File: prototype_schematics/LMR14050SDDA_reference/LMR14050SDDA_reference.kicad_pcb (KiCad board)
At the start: 2 copper layers, 11 parts, among them U1 LMR14050SDDA

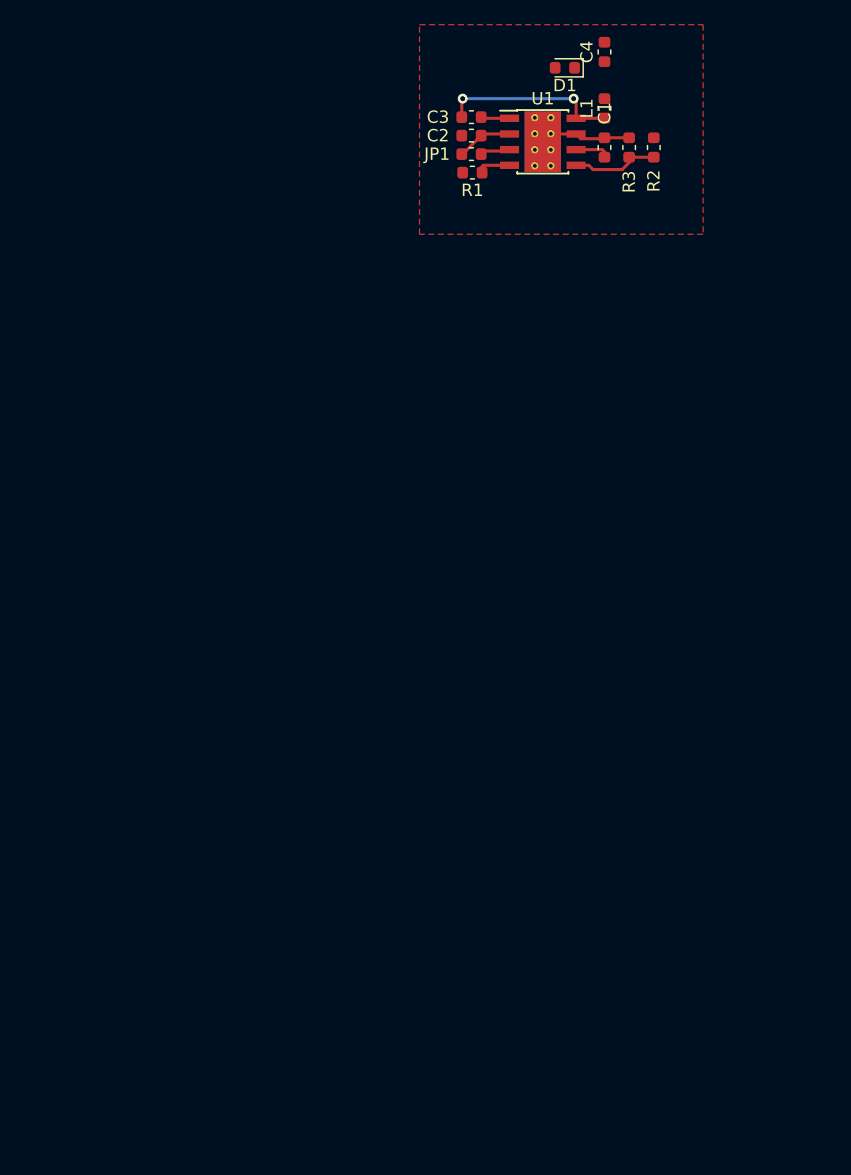
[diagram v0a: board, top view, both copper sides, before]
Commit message: WIP Add power distribution test board rev 1.
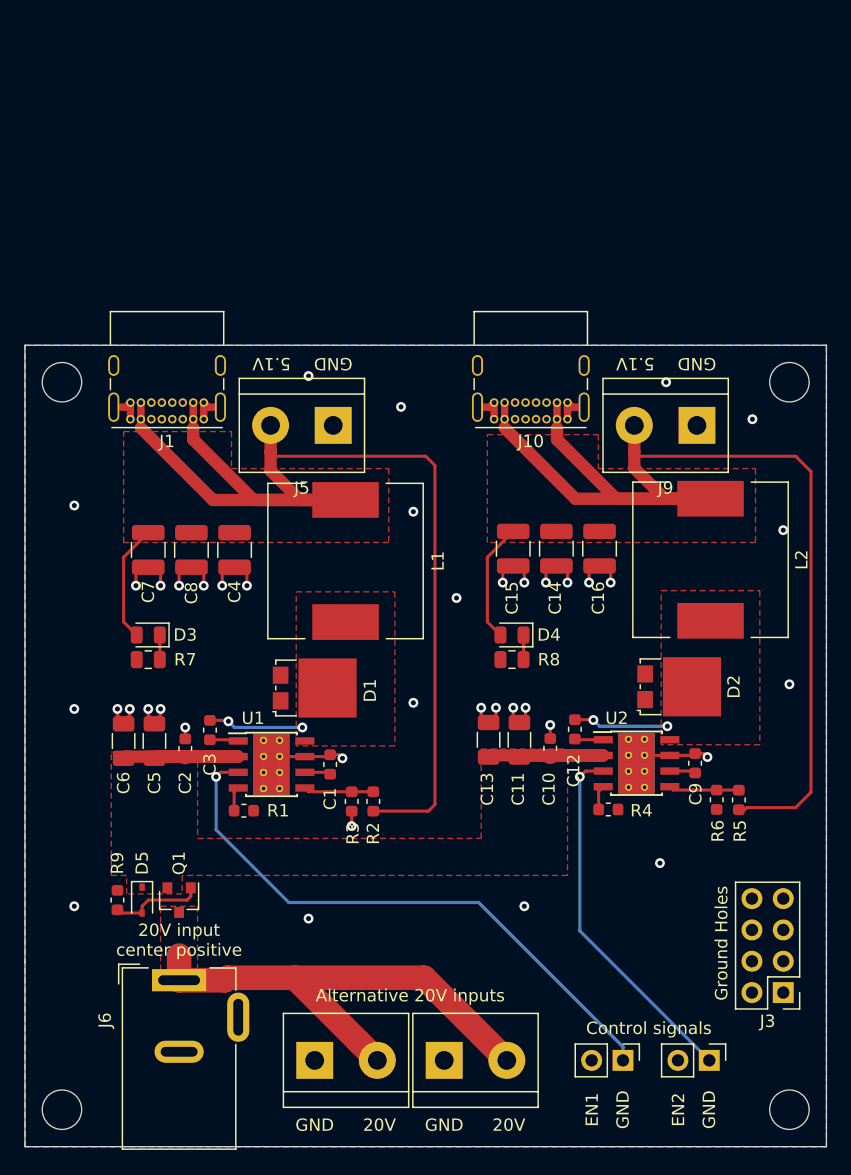
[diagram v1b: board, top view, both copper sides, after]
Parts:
- removed JP1: Jumper, Capacitor_SMD:C_0603_1608Metric
- added C10: 100n, Capacitor_SMD:C_0603_1608Metric, F.Cu at (137.6, 127.7)
- added C11: 4.7uF, Capacitor_SMD:C_1206_3216Metric, F.Cu at (135.1, 127.0)
- added C12: 100n, Capacitor_SMD:C_0603_1608Metric, F.Cu at (139.6, 126.2)
- added C13: 4.7uF, Capacitor_SMD:C_1206_3216Metric, F.Cu at (132.6, 127.0)
- added C14: 47uF, Capacitor_SMD:C_1210_3225Metric, F.Cu at (138.1, 111.5)
- added C15: 47uF, Capacitor_SMD:C_1210_3225Metric, F.Cu at (134.6, 111.5)
- added C16: 47uF, Capacitor_SMD:C_1210_3225Metric, F.Cu at (141.6, 111.5)
- added C5: 4.7uF, Capacitor_SMD:C_1206_3216Metric, F.Cu at (105.5, 127.1)
- added C6: 4.7uF, Capacitor_SMD:C_1206_3216Metric, F.Cu at (103.0, 127.1)
- added C7: 47uF, Capacitor_SMD:C_1210_3225Metric, F.Cu at (105.0, 111.6)
- added C8: 47uF, Capacitor_SMD:C_1210_3225Metric, F.Cu at (108.5, 111.6)
- added C9: 22nF, Capacitor_SMD:C_0603_1608Metric, F.Cu at (149.3, 128.9)
- added D2: D, Package_TO_SOT_SMD:TO-277A, F.Cu at (148.1, 122.7)
- added D3: LED, LED_SMD:LED_0805_2012Metric, F.Cu at (105.0, 118.5)
- added D4: LED, LED_SMD:LED_0805_2012Metric, F.Cu at (134.5, 118.5)
- added D5: 10V, Diode_SMD:D_SOD-323, F.Cu at (104.5, 140.0)
- added H1: MH, MountingHole:MountingHole_3.2mm_M3, F.Cu at (157.0, 98.0)
- added H2: MH, MountingHole:MountingHole_3.2mm_M3, F.Cu at (98.0, 157.0)
- added H3: MH, MountingHole:MountingHole_3.2mm_M3, F.Cu at (98.0, 98.0)
- added H4: MH, MountingHole:MountingHole_3.2mm_M3, F.Cu at (157.0, 157.0)
- added J1: USB_C_Receptacle_USB2.0, Connector_USB:USB_C_Receptacle_GCT_USB4085, F.Cu at (109.5, 101.0)
- added J10: USB_C_Receptacle_USB2.0, Connector_USB:USB_C_Receptacle_GCT_USB4085, F.Cu at (139.0, 101.0)
- added J2: Conn_EN, Connector_PinHeader_2.54mm:PinHeader_1x02_P2.54mm_Vertical, F.Cu at (143.5, 153.0)
- added J3: ground holes, Connector_PinHeader_2.54mm:PinHeader_2x04_P2.54mm_Vertical, F.Cu at (156.5, 147.5)
- added J4: V_in alt, TerminalBlock:TerminalBlock_bornier-2_P5.08mm, F.Cu at (129.0, 153.0)
- added J5: V_out alt, TerminalBlock:TerminalBlock_bornier-2_P5.08mm, F.Cu at (120.0, 101.5)
- added J6: DC_in, Connector_BarrelJack:BarrelJack_Wuerth_6941xx301002, F.Cu at (107.5, 146.5)
- added J7: Conn_EN, Connector_PinHeader_2.54mm:PinHeader_1x02_P2.54mm_Vertical, F.Cu at (150.5, 153.0)
- added J8: V_in alt, TerminalBlock:TerminalBlock_bornier-2_P5.08mm, F.Cu at (118.5, 153.0)
- added J9: V_out alt, TerminalBlock:TerminalBlock_bornier-2_P5.08mm, F.Cu at (149.5, 101.5)
- added L2: 8.2uH, Inductor_SMD:L_Wuerth_WE-PD-Typ-LS, F.Cu at (150.6, 112.4)
- added Q1: IRLML6344TRPBF, Package_TO_SOT_SMD:SOT-23, F.Cu at (107.5, 140.0)
- added R4: 84.5k, Resistor_SMD:R_0603_1608Metric, F.Cu at (142.3, 132.7)
- added R5: 100k, Resistor_SMD:R_0603_1608Metric, F.Cu at (152.9, 131.9)
- added R6: 17.8k, Resistor_SMD:R_0603_1608Metric, F.Cu at (151.1, 131.9)
- added R7: R, Resistor_SMD:R_0805_2012Metric, F.Cu at (105.0, 120.5)
- added R8: R, Resistor_SMD:R_0805_2012Metric, F.Cu at (134.5, 120.5)
- added R9: 100K, Resistor_SMD:R_0603_1608Metric, F.Cu at (102.5, 140.0)
- added U2: LMR14050SDDA, Package_SO:Texas_HSOP-8-1EP_3.9x4.9mm_P1.27mm_ThermalVias, F.Cu at (144.6, 128.9)
- C1: value TBD -> 22nF
- C3: value TDB -> 100n
- C4: value TDB -> 47uF; footprint Capacitor_SMD:C_0603_1608Metric -> Capacitor_SMD:C_1210_3225Metric
- D1: footprint Diode_SMD:D_0603_1608Metric -> Package_TO_SOT_SMD:TO-277A
- L1: value L -> 8.2uH; footprint Inductor_SMD:L_0603_1608Metric -> Inductor_SMD:L_Wuerth_WE-PD-Typ-LS
- R1: value TBD -> 84.5k
- R2: value R -> 100k
- R3: value R -> 17.8k
- moved R2 57.7 mm to (123.2, 132.0), turned to 90 degrees
- moved R3 57.6 mm to (121.5, 132.0), turned to 270 degrees
- moved U1 55.1 mm to (115.0, 129.0)
- moved R1 55.0 mm to (112.8, 132.8), turned to 0 degrees
- moved C2 54.9 mm to (108.0, 127.7), turned to 90 degrees
- moved C1 54.8 mm to (119.8, 129.0)
- moved D1 54.2 mm to (118.5, 122.8), turned to 90 degrees
- moved C3 54.0 mm to (110.0, 126.2), turned to 90 degrees
- moved C4 50.3 mm to (112.0, 111.6), turned to 270 degrees
- moved L1 42.3 mm to (121.0, 112.5)
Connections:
- net /V_FB renamed /V_FB1
- net /V_in renamed /V_in_protected
- net /V_out renamed /V_out1
- D1 pad 1: Net-(C3-Pad2) -> GND
- U1 pad 3: /enable_signal -> /en_signal1
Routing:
- net /V_out2: track 0.00 -> 106.4 mm
- net /V_out1: track 0.00 -> 105.3 mm
- net GND: track 7.45 -> 64.6 mm, vias 0 -> 40
- net /en_signal1: track 0.00 -> 47.6 mm, vias 0 -> 1
- net /V_in: track 0.00 -> 40.9 mm
- net /V_in_protected: track 4.55 -> 41.2 mm
- net /en_signal2: track 0.00 -> 29.4 mm, vias 0 -> 1
- net Net-(C12-Pad2): track 0.00 -> 7.72 mm, vias 0 -> 2
- net Net-(D5-Pad2): track 0.00 -> 7.64 mm
- net Net-(C3-Pad2): track 14.5 -> 7.74 mm
- net /V_FB2: track 0.00 -> 5.72 mm
- net /enable_signal: track 2.45 -> 0.00 mm
- net Net-(C12-Pad1): track 0.00 -> 2.32 mm
- net Net-(C9-Pad1): track 0.00 -> 2.11 mm
- net Net-(R4-Pad1): track 0.00 -> 2.00 mm
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- added copper zone on F.Cu, net /V_in
- added copper zone on F.Cu, net /V_in_protected
- added copper zone on F.Cu, net /V_out1
- added copper zone on F.Cu, net /V_out2
- added copper zone on B.Cu, net GND
- added copper zone on F.Cu, net Net-(C12-Pad2)
- added copper zone on F.Cu, net Net-(C3-Pad2)
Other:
- board outline added: 65 x 65 mm
- rule via_min_drill: 0.3 -> 0.2
- rule via_min_size: 0.4 -> 0.45
- board text added: "20V"
- board text added: "20V input center positive"
- board text added: "5.1V"
- board text added: "Alternative 20V inputs"
- board text added: "Control signals"
- board text added: "EN1"
- board text added: "EN2"
- board text added: "GND"
- board text added: "Ground Holes"
- board text added: "Special Computing Machine Power Distribution Test Board (rev. 1) Verneri Hirvonen (@asdvek) 2020"

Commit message: Final changes for ordering.
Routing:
- net Net-(C3-Pad2): track 7.74 -> 17.5 mm
- net GND: track 64.6 -> 73.6 mm, vias 40 -> 38
- net Net-(C12-Pad2): track 7.72 -> 15.6 mm
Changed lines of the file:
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@@
   (general
     (thickness 1.6)
-    (drawings 24)
-    (tracks 236)
+    (drawings 26)
+    (tracks 245)
     (zones 0)
     (modules 49)
@@
       (outputformat 1)
       (mirror false)
-      (drillshape 1)
+      (drillshape 0)
       (scaleselection 1)
-      (outputdirectory ""))
+      (outputdirectory "plots/"))
   )
   (net 0 "")
@@
     (tags resistor)
     (attr smd)
-    (fp_text reference R4 (at 2.6875 0.1) (layer F.SilkS)
+    (fp_text reference R4 (at -2.8125 0.1) (layer F.SilkS)
       (effects (font (size 1 1) (thickness 0.15)))
     )
@@
     (tags resistor)
     (attr smd)
-    (fp_text reference R1 (at 2.7875 0) (layer F.SilkS)
+    (fp_text reference R1 (at -2.75 0) (layer F.SilkS)
       (effects (font (size 1 1) (thickness 0.15)))
     )
@@
     )
   )
+  (gr_poly (pts (xy 146.4 133.8) (xy 144 133.8) (xy 144 131.6) (xy 146.4 131.6)) (layer F.Mask) (width 0.1))
+  (gr_poly (pts (xy 116.5 134) (xy 114.5 134) (xy 114.5 131.5) (xy 116.5 131.5)) (layer F.Mask) (width 0.1))
   (gr_poly (pts (xy 160 138) (xy 155.5 138) (xy 155.5 133.5) (xy 160 133.5)) (layer B.Mask) (width 0.1))
   (gr_poly (pts (xy 160 138) (xy 155.5 138) (xy 155.5 133.5) (xy 160 133.5)) (layer F.Mask) (width 0.1))
-  (gr_text "Special Computing Machine\nPower Distribution Test Board (rev. 1)\nVerneri Hirvonen (@asdvek) 2020" (at 153 105.5 90) (layer B.SilkS)
+  (gr_text "Special Computing Machine\nPower Distribution Test Board (rev. 1)\nVerneri Hirvonen (@asdvek) 2020" (at 99.6 152.4 270) (layer B.SilkS)
     (effects (font (size 1 1) (thickness 0.15)) (justify left mirror))
   )
@@
   (segment (start 147.3 128.265) (end 145.235 128.265) (width 0.25) (layer F.Cu) (net 1))
   (via (at 99 108) (size 0.8) (drill 0.4) (layers F.Cu B.Cu) (net 1))
-  (via (at 99 124.5) (size 0.8) (drill 0.4) (layers F.Cu B.Cu) (net 1))
-  (via (at 99 140.5) (size 0.8) (drill 0.4) (layers F.Cu B.Cu) (net 1))
   (via (at 118 141.5) (size 0.8) (drill 0.4) (layers F.Cu B.Cu) (net 1))
   (via (at 135.5 140.5) (size 0.8) (drill 0.4) (layers F.Cu B.Cu) (net 1))
@@
   (via (at 126.5 124) (size 0.8) (drill 0.4) (layers F.Cu B.Cu) (net 1))
   (via (at 126.5 108.5) (size 0.8) (drill 0.4) (layers F.Cu B.Cu) (net 1))
+  (segment (start 115 129) (end 115 131.5) (width 2) (layer F.Cu) (net 1))
+  (segment (start 115 131.5) (end 116.5 133) (width 2) (layer F.Cu) (net 1))
+  (segment (start 144.6 131.340002) (end 146 132.740002) (width 2) (layer F.Cu) (net 1))
+  (segment (start 144.6 128.9) (end 144.6 131.340002) (width 2) (layer F.Cu) (net 1))
   (segment (start 119.5975 129.635) (end 119.75 129.7875) (width 0.25) (layer F.Cu) (net 2))
   (segment (start 117.7 129.635) (end 119.5975 129.635) (width 0.25) (layer F.Cu) (net 2))
@@
   (segment (start 116.87999 146.29999) (end 127.37999 146.29999) (width 2) (layer F.Cu) (net 3))
   (segment (start 107.5 146.5) (end 107.5 144.5) (width 2) (layer F.Cu) (net 3))
-  (segment (start 137.81 128.265) (end 137.6 128.475) (width 1) (layer F.Cu) (net 35))
-  (segment (start 141.9 128.265) (end 137.81 128.265) (width 1) (layer F.Cu) (net 35))
-  (segment (start 135.235 128.265) (end 135.1 128.4) (width 1) (layer F.Cu) (net 35))
-  (segment (start 141.9 128.265) (end 135.235 128.265) (width 1) (layer F.Cu) (net 35))
-  (segment (start 132.735 128.265) (end 132.6 128.4) (width 1) (layer F.Cu) (net 35))
-  (segment (start 141.9 128.265) (end 132.735 128.265) (width 1) (layer F.Cu) (net 35))
   (via (at 117.5 126) (size 0.8) (drill 0.4) (layers F.Cu B.Cu) (net 4))
   (segment (start 117.5 126) (end 112 126) (width 0.25) (layer B.Cu) (net 4))
@@
   (segment (start 111.425 125.425) (end 111.5 125.5) (width 0.25) (layer F.Cu) (net 4))
   (segment (start 110 125.425) (end 111.425 125.425) (width 0.25) (layer F.Cu) (net 4))
+  (segment (start 119.54 122.8) (end 119.54 120.86) (width 1) (layer F.Cu) (net 4))
+  (segment (start 119.54 122.8) (end 119.54 120.06) (width 1) (layer F.Cu) (net 4))
+  (segment (start 121 117.45) (end 121 119.4) (width 1) (layer F.Cu) (net 4))
+  (segment (start 119.54 122.8) (end 119.54 125.94) (width 1) (layer F.Cu) (net 4))
   (segment (start 112.205 127) (end 112.3 127.095) (width 0.25) (layer F.Cu) (net 5))
   (segment (start 110 127) (end 112.205 127) (width 0.25) (layer F.Cu) (net 5))
@@
   (via (at 147.1 125.9) (size 0.8) (drill 0.4) (layers F.Cu B.Cu) (net 17))
   (segment (start 141.6 125.9) (end 147.1 125.9) (width 0.25) (layer B.Cu) (net 17))
+  (segment (start 149.1 122.7) (end 149.1 125.9) (width 1) (layer F.Cu) (net 17))
+  (segment (start 150.6 117.35) (end 150.6 119.2) (width 1) (layer F.Cu) (net 17))
+  (segment (start 149.1 122.7) (end 149.1 119.9) (width 1) (layer F.Cu) (net 17))
   (segment (start 139.6575 126.995) (end 139.6 126.9375) (width 0.25) (layer F.Cu) (net 18))
   (segment (start 141.9 126.995) (end 139.6575 126.995) (width 0.25) (layer F.Cu) (net 18))
@@
   (segment (start 105.9375 120.5) (end 105.9375 118.5) (width 0.25) (layer F.Cu) (net 33))
   (segment (start 135.4375 120.495) (end 135.4375 118.5) (width 0.25) (layer F.Cu) (net 34))
+  (segment (start 137.81 128.265) (end 137.6 128.475) (width 1) (layer F.Cu) (net 35))
+  (segment (start 141.9 128.265) (end 137.81 128.265) (width 1) (layer F.Cu) (net 35))
+  (segment (start 135.235 128.265) (end 135.1 128.4) (width 1) (layer F.Cu) (net 35))
+  (segment (start 141.9 128.265) (end 135.235 128.265) (width 1) (layer F.Cu) (net 35))
+  (segment (start 132.735 128.265) (end 132.6 128.4) (width 1) (layer F.Cu) (net 35))
+  (segment (start 141.9 128.265) (end 132.735 128.265) (width 1) (layer F.Cu) (net 35))
   (segment (start 108.135 128.365) (end 108 128.5) (width 1) (layer F.Cu) (net 35))
   (segment (start 112.3 128.365) (end 108.135 128.365) (width 1) (layer F.Cu) (net 35))

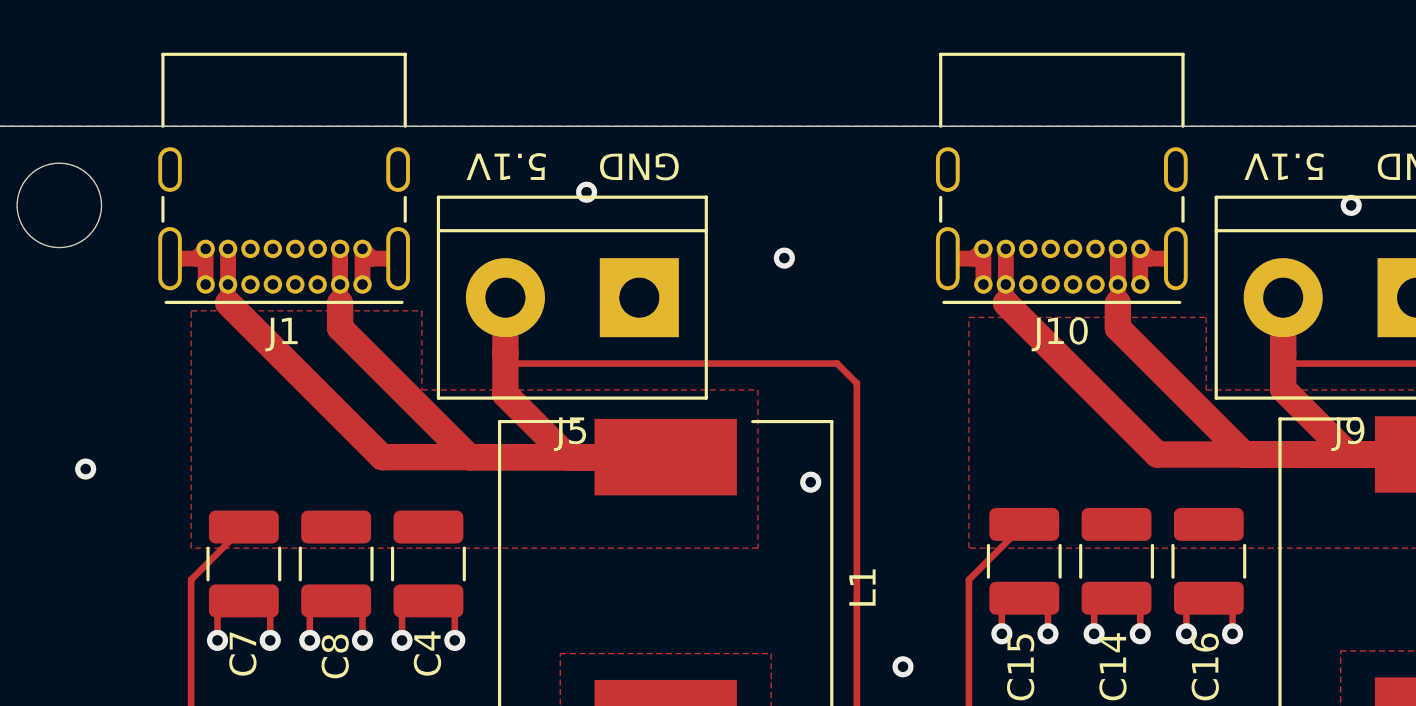
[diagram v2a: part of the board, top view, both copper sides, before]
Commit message: Change USB C receptacle to a component that's in stock.
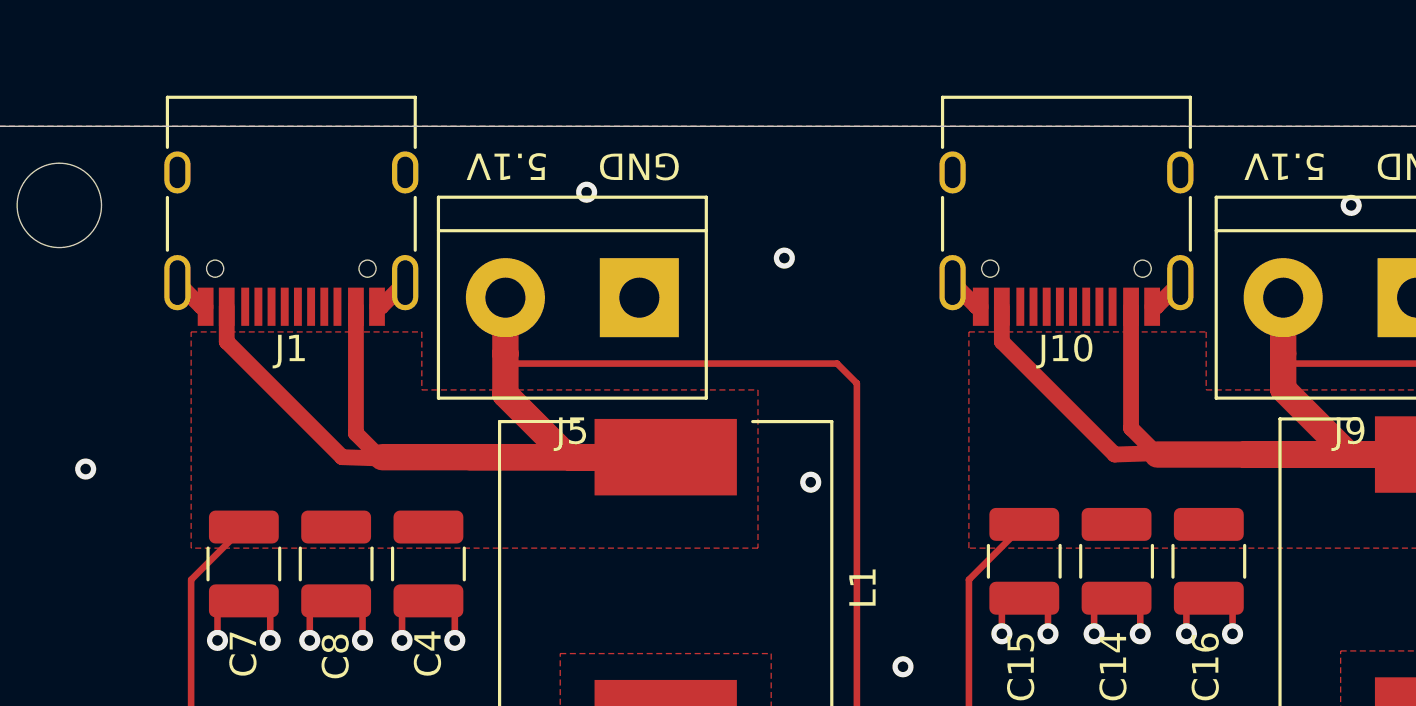
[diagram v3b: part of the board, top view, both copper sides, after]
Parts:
- J1, J10: footprint Connector_USB:USB_C_Receptacle_GCT_USB4085 -> Connector_USB:USB_C_Receptacle_HRO_TYPE-C-31-M-12
- R7, R8: value R -> 3.3k
- moved J10 4.25 mm to (136.2, 97.8)
- moved J1 4.19 mm to (106.8, 97.8)
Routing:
- net GND: track 73.6 -> 68.0 mm
- net /V_out1: track 105.3 -> 100.2 mm
- net /V_out2: track 106.4 -> 101.4 mm
